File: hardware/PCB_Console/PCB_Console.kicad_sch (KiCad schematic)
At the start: 67 parts, among them J1 0R, J1 USB_C_Receptacle_PowerOnly_6P, J2 CP2102 module, Q1 2N3904, Q2 2N3904, SW1 SW_MEC_5E, SW2 SW_MEC_5E, SW3 SW_MEC_5E, SW4 SW_MEC_5E, SW5 SW_MEC_5E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

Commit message: routing and placment, few edits on schematics
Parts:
- removed 3_3V_tp1, IO0_tp1: TestPoint, TestPoint:TestPoint_Pad_D1.0mm, symbol Connector:TestPoint
- removed BAT+1, BAT-1: MountingHole_Pad_MP, TestPoint:TestPoint_Pad_2.5x2.5mm, symbol Mechanical:MountingHole_Pad_MP
- removed BT1: Battery_Cell, symbol Device:Battery_Cell
- added TP2: Battery-, TestPoint:TestPoint_THTPad_D1.5mm_Drill0.7mm, symbol Connector:TestPoint_Alt
- added TP3: Battery+, TestPoint:TestPoint_THTPad_D1.5mm_Drill0.7mm, symbol Connector:TestPoint_Alt
- GND_tp1: footprint TestPoint:TestPoint_Pad_D1.0mm -> TestPoint:TestPoint_Pad_D1.5mm
- renumbered J1 to J5
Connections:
- net Bat+: now also TP3.1
- net GND: now also TP2.1

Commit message: routing next step
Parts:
- removed EN_ESP_tp1: TestPoint, TestPoint:TestPoint_Pad_D1.0mm, symbol Connector:TestPoint
- removed R10: 0R, Resistor_SMD:R_1206_3216Metric_Pad1.30x1.75mm_HandSolder, symbol Device:R
- added R12, R13: 0, Resistor_SMD:R_1206_3216Metric_Pad1.30x1.75mm_HandSolder, symbol Device:R
- D2, D3: footprint Diode_SMD:D_SOD-123 -> Diode_SMD:D_0805_2012Metric_Pad1.15x1.40mm_HandSolder
- SW1, SW2: footprint Library:SW_Push_12x12_aliexpress -> TS04-66-95-BK-100-SMT:SW_TS04-66-95-BK-100-SMT
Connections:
- net 3_3V_AMSVO: now also R12.1, R12.2
- net DTR_BL: now also C8.2
- net GND: now also R13.1, R13.2
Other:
- note added: "ENABLE"
- note removed: "RESET"
- moved on the sheet: R8

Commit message: routing czesc dalsza, power manager system wmiare polaczony
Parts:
- SW1: footprint TS04-66-95-BK-100-SMT:SW_TS04-66-95-BK-100-SMT -> components_lib:SW_TS04-66-95-BK-100-SMT
- SW9: footprint Library:SW_Push_12x12_aliexpress -> TS04-66-95-BK-100-SMT:SW_TS04-66-95-BK-100-SMT
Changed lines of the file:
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@@
 			)
 		)
-		(property "Footprint" "Library:SW_Push_12x12_aliexpress"
+		(property "Footprint" "TS04-66-95-BK-100-SMT:SW_TS04-66-95-BK-100-SMT"
 			(at 95.25 129.54 0)
 			(effects
@@
 			)
 		)
-		(property "Footprint" "TS04-66-95-BK-100-SMT:SW_TS04-66-95-BK-100-SMT"
+		(property "Footprint" "components_lib:SW_TS04-66-95-BK-100-SMT"
 			(at 194.31 33.02 0)
 			(effects

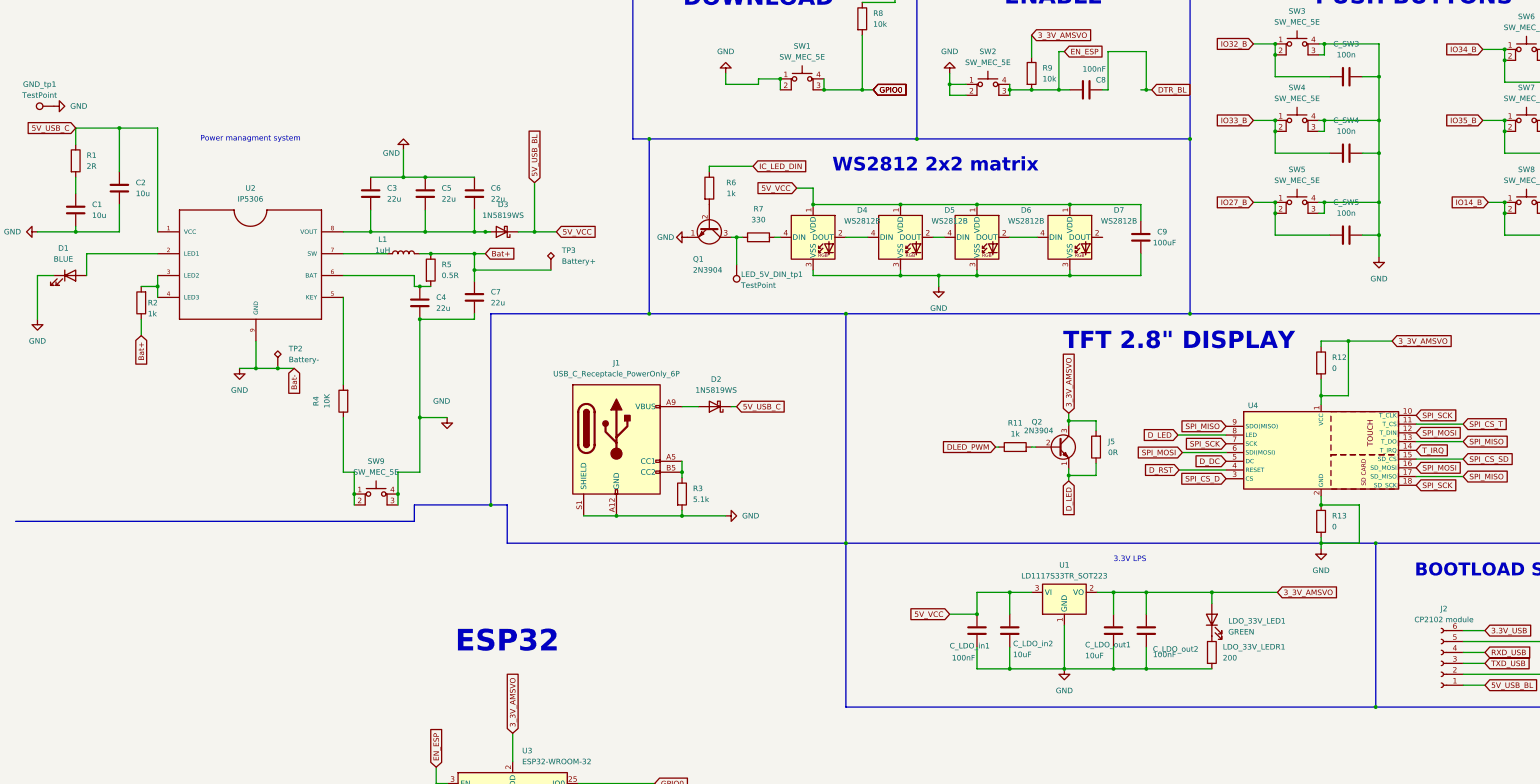
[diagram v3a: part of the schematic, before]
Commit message: routing on 2l done, need to check, text and logo added
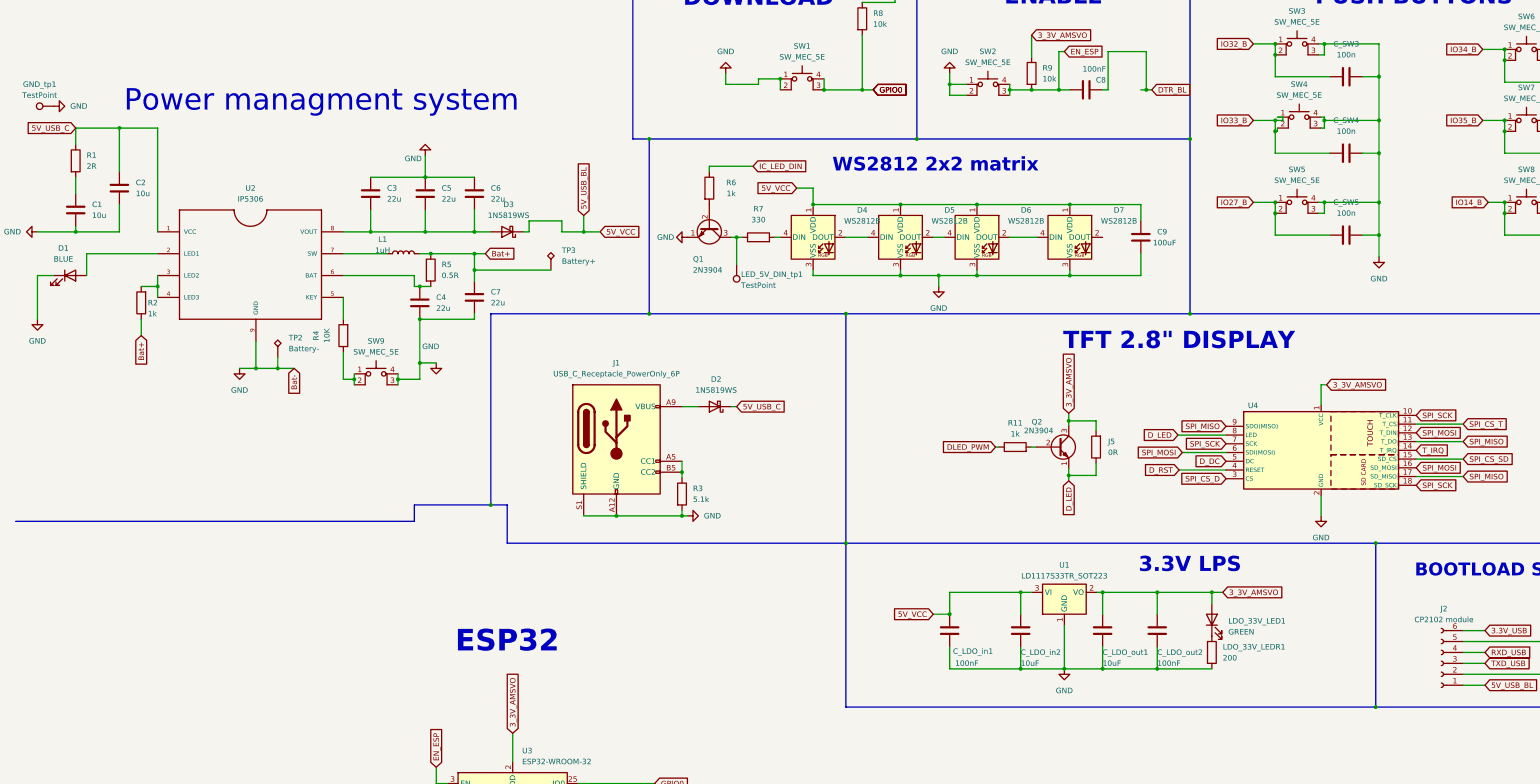
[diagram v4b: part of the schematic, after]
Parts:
- removed R12, R13: 0, Resistor_SMD:R_1206_3216Metric_Pad1.30x1.75mm_HandSolder, symbol Device:R
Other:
- moved on the sheet: C_LDO_in1, C_LDO_in2, C_LDO_out1, C_LDO_out2, D3, R4, SW4, SW9, TP2

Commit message: pull up resistors added; level shifter fixed-> tested using sim LTspice
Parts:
- added R10, R12: 10k, Resistor_SMD:R_1206_3216Metric_Pad1.30x1.75mm_HandSolder, symbol Device:R
- R7: value 330 -> 10k
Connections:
- net 5V_USB_BL: now also R10.2
- net GND: now also R7.2, R12.2; no longer SW6.3 (K), SW6.4 (A), SW7.3 (K), SW7.4 (A)
- net at LED_5V_DIN_tp1.1, Q1.3 (C): now also D4.4 (DIN), R10.1; no longer R7.1
- new net: R12.1, SW6.3 (K), SW6.4 (A)
- new net: R7.1, SW7.3 (K), SW7.4 (A)
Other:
- moved on the sheet: C_SW3, C_SW4, C_SW5, C_SW6, C_SW7, C_SW8, D2, J1, LED_5V_DIN_tp1, R3, R6, SW3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
